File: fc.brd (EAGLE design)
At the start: 55 x 40 mm, 72 parts, among them IC1 BN055, J1 USBC, U1 LMZ21700, U2 ATMEGA2560-16AU100A-M, U4 FT230XQ, Y1 16MHz, Y2 32.768kHz

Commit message: atmega breakout cleanup
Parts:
- moved S1 37.6 mm to (12.4, 43.5)
- moved R3 36.2 mm to (12.2, 46.6)
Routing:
- net !RESET: track 38.8 -> 9.92 mm, vias 3 -> 1
- net +3V3: track 138.4 -> 128.1 mm
- net BNO_INT: track 26.6 -> 23.1 mm
- net PPM2: track 29.2 -> 32.3 mm
- net PPM0: track 37.6 -> 39.5 mm
- net PPM1: track 33.8 -> 35.3 mm
- net MOSI: track 18.6 -> 19.8 mm, vias 0 -> 1
- net SCK: track 18.2 -> 17.3 mm
- net PPM7: track 36.0 -> 35.3 mm
- net USB_TX: track 28.2 -> 27.5 mm
- net PPM3: track 29.3 -> 28.7 mm

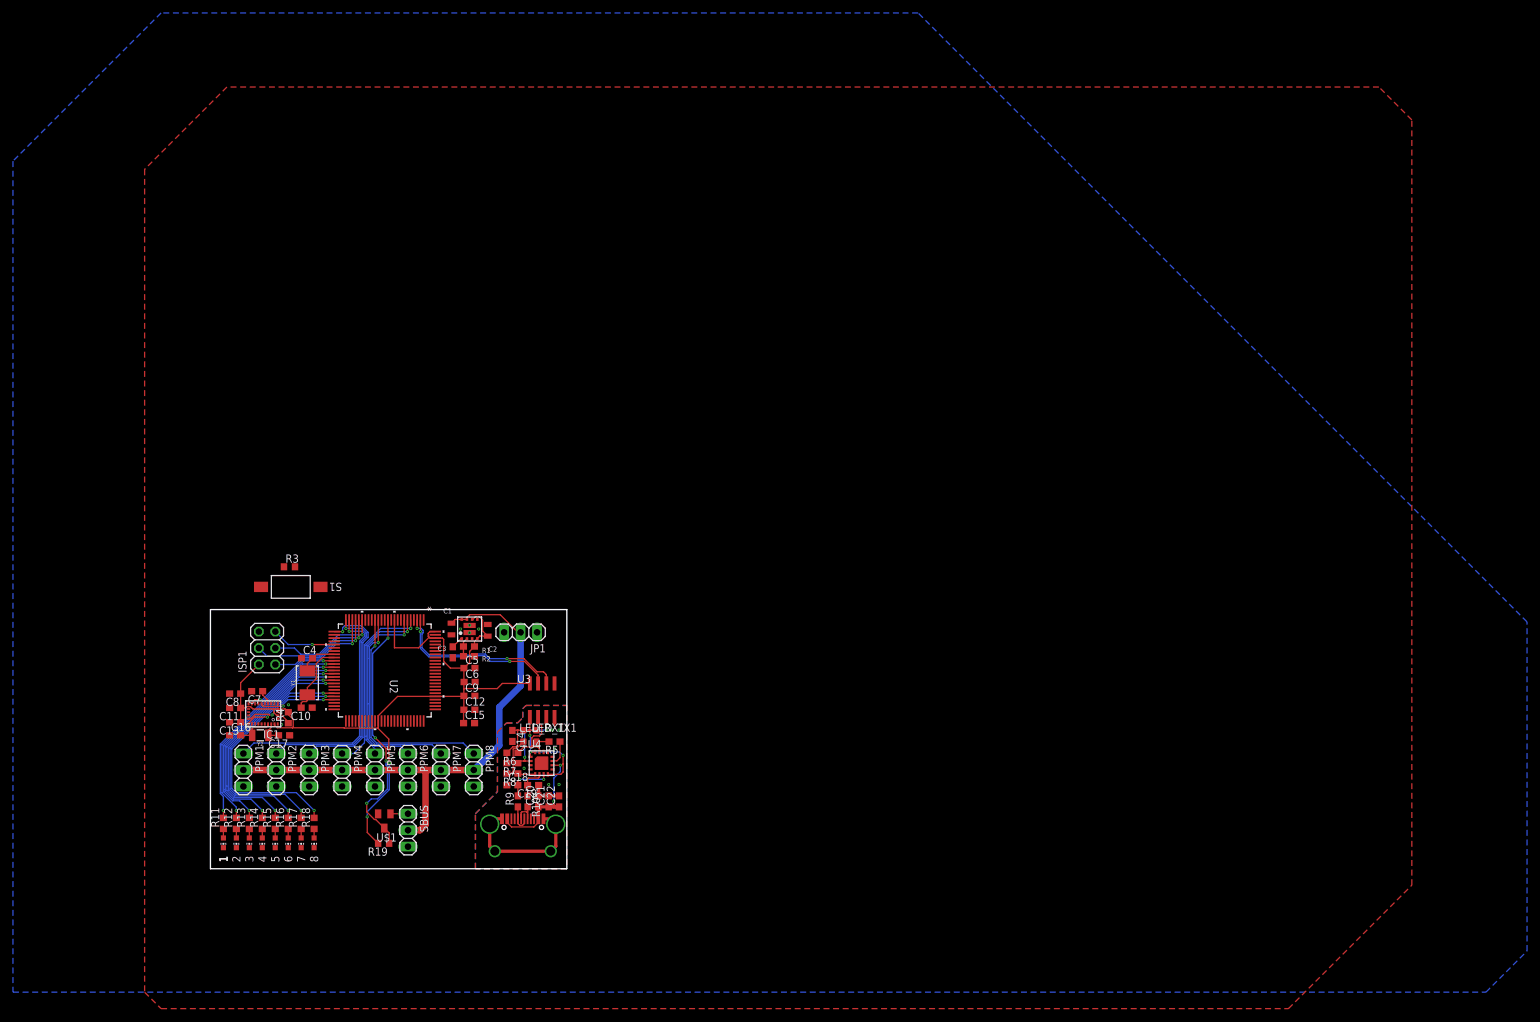
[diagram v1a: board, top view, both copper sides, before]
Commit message: isp, reset button, gnd polygon
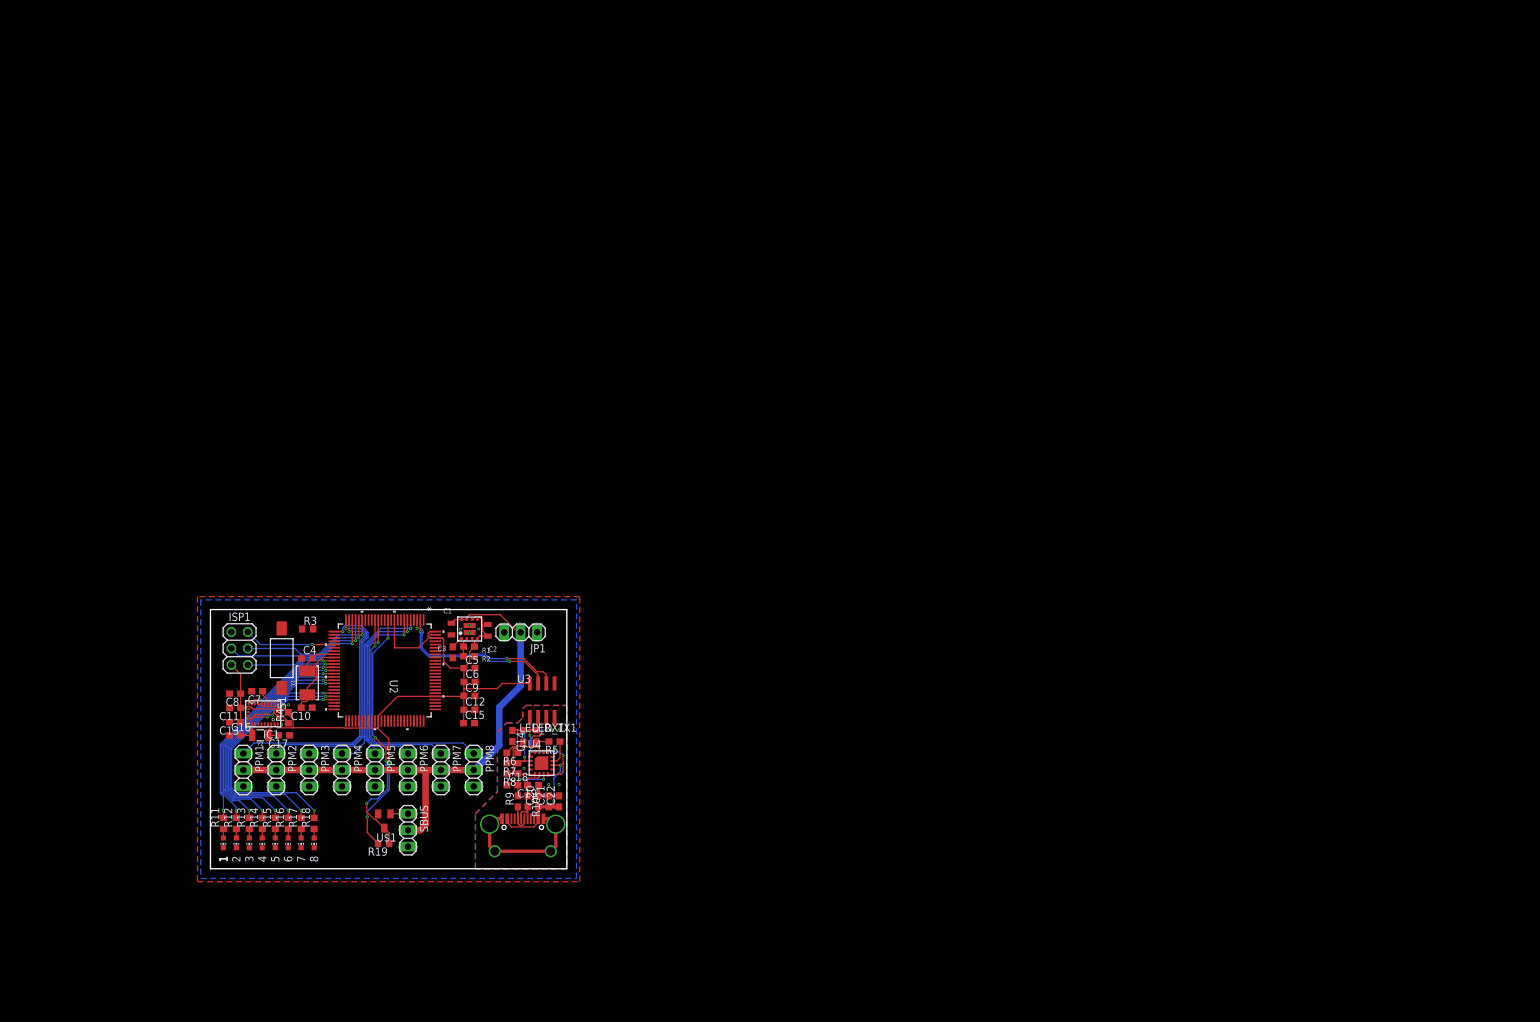
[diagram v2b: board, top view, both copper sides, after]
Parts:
- moved S1 11.1 mm to (11.0, 32.5), turned to 90 degrees
- moved R3 10.0 mm to (15.0, 37.0)
- moved ISP1 4.24 mm to (4.50, 34.0)
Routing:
- net MISO: track 17.1 -> 21.4 mm
- net SCK: track 17.3 -> 21.5 mm
- net MOSI: track 19.8 -> 24.0 mm
- net !RESET: track 9.92 -> 14.1 mm
- net +3V3: track 128.1 -> 127.5 mm
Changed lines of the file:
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@@
 <layer number="45" name="Holes" color="7" fill="1" visible="yes" active="yes"/>
 <layer number="46" name="Milling" color="3" fill="1" visible="no" active="yes"/>
-<layer number="47" name="Measures" color="7" fill="1" visible="no" active="yes"/>
+<layer number="47" name="Measures" color="7" fill="1" visible="yes" active="yes"/>
 <layer number="48" name="Document" color="7" fill="1" visible="no" active="yes"/>
 <layer number="49" name="Reference" color="7" fill="1" visible="no" active="yes"/>
@@
 <wire x1="55" y1="40" x2="0" y2="40" width="0" layer="20"/>
 <wire x1="0" y1="40" x2="0" y2="0" width="0" layer="20"/>
-<dimension x1="0" y1="0" x2="55.88" y2="0" x3="27.94" y3="66.04" textsize="1.778" layer="47"/>
-<dimension x1="0" y1="0" x2="0.1524" y2="41.148" x3="63.199978125" y3="20.34020625" textsize="1.778" layer="47"/>
 <text x="2" y="2" size="1.27" layer="21" rot="R90" align="center-right">1</text>
 <text x="2" y="2" size="1.27" layer="21" rot="R90" align="center-right">1</text>
@@
 <text x="14" y="2" size="1.27" layer="21" rot="R90" align="center-right">7</text>
 <text x="16" y="2" size="1.27" layer="21" rot="R90" align="center-right">8</text>
+<dimension x1="0" y1="0" x2="55" y2="0" x3="27.5" y3="-5" textsize="1.4224" layer="47" dtype="horizontal" width="0.1"/>
+<dimension x1="0" y1="40" x2="0" y2="0" x3="-14.5" y3="20" textsize="1.4224" layer="47" dtype="vertical" width="0.1"/>
 </plain>
 <attributes>
@@
 <attribute name="VENDOR" value="Atmel" x="26.9" y="30.6" size="1.778" layer="27" rot="R270" display="off"/>
 </element>
-<element name="ISP1" library="pinhead" library_urn="urn:adsk.eagle:library:325" package="2X03" package3d_urn="urn:adsk.eagle:package:22462/2" value="" x="8.7436" y="34.0612" smashed="yes" rot="R90">
-<attribute name="NAME" x="5.5686" y="30.2512" size="1.27" layer="25" ratio="10" rot="R90"/>
-<attribute name="VALUE" x="13.1886" y="30.2512" size="1.27" layer="27" rot="R90"/>
+<element name="ISP1" library="pinhead" library_urn="urn:adsk.eagle:library:325" package="2X03" package3d_urn="urn:adsk.eagle:package:22462/2" value="" x="4.5" y="34" smashed="yes" rot="R90">
+<attribute name="NAME" x="4.5" y="38.25" size="1.27" layer="25" ratio="10" align="bottom-center"/>
+<attribute name="VALUE" x="8.945" y="30.19" size="1.27" layer="27" rot="R90"/>
 </element>
 <element name="Y1" library="SparkFun-Clocks" library_urn="urn:adsk.eagle:library:511" package="CRYSTAL-SMD-5X3.2-2PAD" package3d_urn="urn:adsk.eagle:package:37520/1" value="16MHz" x="14.954" y="28.7012" smashed="yes" rot="R90">
@@
 <attribute name="VALUE" x="39.3274" y="24.7778" size="1.27" layer="27"/>
 </element>
-<element name="R3" library="resistor" library_urn="urn:adsk.eagle:library:348" package="R0603" package3d_urn="urn:adsk.eagle:package:23555/2" value="10k" x="12.2" y="46.6" smashed="yes">
-<attribute name="NAME" x="11.565" y="47.235" size="1.27" layer="25"/>
-<attribute name="VALUE" x="11.565" y="44.695" size="1.27" layer="27"/>
-</element>
-<element name="S1" library="switch" package="SWITCH_FSMSM" value="FSMSM" x="12.4" y="43.5" smashed="yes" rot="R180">
-<attribute name="MANUFACTURER_PART_NUMBER" value="FSMSM" x="12.4" y="43.5" size="1.778" layer="27" rot="R180" display="off"/>
-<attribute name="NAME" x="20.2994" y="44.135" size="1.27" layer="25" ratio="6" rot="SR180"/>
-<attribute name="VENDOR" value="TE Connectivity" x="12.4" y="43.5" size="1.778" layer="27" rot="R180" display="off"/>
+<element name="R3" library="resistor" library_urn="urn:adsk.eagle:library:348" package="R0603" package3d_urn="urn:adsk.eagle:package:23555/2" value="10k" x="15" y="37" smashed="yes">
+<attribute name="NAME" x="14.365" y="37.635" size="1.27" layer="25"/>
+<attribute name="VALUE" x="14.365" y="35.095" size="1.27" layer="27"/>
+</element>
+<element name="S1" library="switch" package="SWITCH_FSMSM" value="FSMSM" x="11" y="32.5" smashed="yes" rot="R90">
+<attribute name="MANUFACTURER_PART_NUMBER" value="FSMSM" x="11" y="32.5" size="1.778" layer="27" rot="R90" display="off"/>
+<attribute name="NAME" x="11.635" y="24.6006" size="1.27" layer="25" ratio="6" rot="SR90"/>
+<attribute name="VENDOR" value="TE Connectivity" x="11" y="32.5" size="1.778" layer="27" rot="R90" display="off"/>
 </element>
 <element name="C19" library="SparkFun-Capacitors" library_urn="urn:adsk.eagle:library:510" package="0603" package3d_urn="urn:adsk.eagle:package:37414/1" value="47pF" x="49.8" y="12.9" smashed="yes" rot="R180">
@@
 <contactref element="S1" pad="2"/>
 <wire x1="19.1022" y1="34.6" x2="15.6972" y2="34.6" width="0.1524" layer="1"/>
-<wire x1="10.0136" y1="36.6012" x2="12.0148" y2="34.6" width="0.1524" layer="16"/>
-<wire x1="12.0148" y1="34.6" x2="15.6972" y2="34.6" width="0.1524" layer="16"/>
+<wire x1="5.77" y1="36.54" x2="7.71" y2="34.6" width="0.1524" layer="16"/>
+<wire x1="7.71" y1="34.6" x2="15.6972" y2="34.6" width="0.1524" layer="16"/>
 <via x="15.6972" y="34.6" extent="1-16" drill="0.2"/>
-<wire x1="7.81" y1="43.5" x2="11.35" y2="46.6" width="0" layer="19" extent="1-1"/>
-<wire x1="10.0136" y1="36.6012" x2="7.81" y2="43.5" width="0" layer="19" extent="1-1"/>
+<wire x1="11" y1="37.09" x2="14.15" y2="37" width="0" layer="19" extent="1-1"/>
+<wire x1="5.77" y1="36.54" x2="11" y2="37.09" width="0" layer="19" extent="1-1"/>
 </signal>
 <signal name="+5V">
@@
 <contactref element="LED8" pad="C"/>
 <polygon width="0.1524" layer="1" rank="6">
-<vertex x="-10.16" y="107.95"/>
-<vertex x="-10.16" y="-19.05"/>
-<vertex x="-7.62" y="-21.59"/>
-<vertex x="166.37" y="-21.59"/>
-<vertex x="185.42" y="-2.54"/>
-<vertex x="185.42" y="115.57"/>
-<vertex x="180.34" y="120.65"/>
-<vertex x="2.54" y="120.65"/>
+<vertex x="-2" y="42"/>
+<vertex x="-2" y="-2"/>
+<vertex x="57" y="-2"/>
+<vertex x="57" y="42"/>
 </polygon>
 <polygon width="0.1524" layer="16" rank="6">
-<vertex x="-13.97" y="125.73"/>
-<vertex x="-30.48" y="109.22"/>
-<vertex x="-30.48" y="-19.05"/>
-<vertex x="196.85" y="-19.05"/>
-<vertex x="203.2" y="-12.7"/>
-<vertex x="203.2" y="38.1"/>
-<vertex x="109.22" y="132.08"/>
-<vertex x="-7.62" y="132.08"/>
+<vertex x="-1.5" y="41.5"/>
+<vertex x="-1.5" y="-1.5"/>
+<vertex x="56.5" y="-1.5"/>
+<vertex x="56.5" y="41.5"/>
 </polygon>
 <contactref element="JP1" pad="1"/>
@@
 <via x="40" y="36.4" extent="1-16" drill="0.2"/>
 <via x="40" y="37.6" extent="1-16" drill="0.2"/>
-<wire x1="16.99" y1="43.5" x2="19.1022" y2="33.6" width="0" layer="19" extent="1-1"/>
+<wire x1="11" y1="27.91" x2="19.1022" y2="33.6" width="0" layer="19" extent="1-1"/>
 </signal>
 <signal name="USB_RX">
@@
 <wire x1="25.8704" y1="21.6704" x2="25.8292" y2="21.7116" width="0.2032" layer="1"/>
 <wire x1="25.8292" y1="21.7116" x2="20.67679375" y2="21.7116" width="0.2032" layer="1"/>
-<wire x1="7.4736" y1="31.5212" x2="4.66" y2="28.7076" width="0.2032" layer="1"/>
-<wire x1="4.66" y1="28.7076" x2="4.66" y2="27.03" width="0.2032" layer="1"/>
+<wire x1="3.23" y1="31.46" x2="4.66" y2="30.03" width="0.2032" layer="1"/>
+<wire x1="4.66" y1="30.03" x2="4.66" y2="27.03" width="0.2032" layer="1"/>
 <wire x1="25.9" y1="22.8022" x2="25.9" y2="21.7" width="0.2032" layer="1"/>
 <wire x1="25.9" y1="21.7" x2="25.8704" y2="21.6704" width="0.2032" layer="1"/>
@@
 <wire x1="41.9984" y1="38.37670625" x2="41.47350625" y2="38.9016" width="0.2032" layer="1"/>
 <wire x1="41.9984" y1="36.7016" x2="41.9984" y2="38.37670625" width="0.2032" layer="1"/>
-<wire x1="19.1022" y1="34.1" x2="13.05" y2="46.6" width="0" layer="19" extent="1-1"/>
+<wire x1="19.1022" y1="34.1" x2="15.85" y2="37" width="0" layer="19" extent="1-1"/>
 <wire x1="28.4" y1="34.1" x2="19.1022" y2="34.1" width="0" layer="19" extent="1-1"/>
 </signal>
@@
 <contactref element="U2" pad="22"/>
 <wire x1="16.94510625" y1="32.6048" x2="14.1794625" y2="32.6048" width="0.1524" layer="16"/>
-<wire x1="10.0136" y1="31.5212" x2="13.0958625" y2="31.5212" width="0.1524" layer="16"/>
-<wire x1="13.0958625" y1="31.5212" x2="14.1794625" y2="32.6048" width="0.1524" layer="16"/>
+<wire x1="5.77" y1="31.46" x2="13.0346625" y2="31.46" width="0.1524" layer="16"/>
+<wire x1="13.0346625" y1="31.46" x2="14.1794625" y2="32.6048" width="0.1524" layer="16"/>
 <via x="22.4" y="35.2" extent="1-16" drill="0.2"/>
 <wire x1="22.4" y1="38.3978" x2="22.4" y2="35.2" width="0.1524" layer="1"/>
@@
 <contactref element="ISP1" pad="3"/>
 <contactref element="U2" pad="20"/>
-<wire x1="10.0136" y1="34.0612" x2="12.9692" y2="34.0612" width="0.1524" layer="16"/>
-<wire x1="12.9692" y1="34.0612" x2="13.9208" y2="33.1096" width="0.1524" layer="16"/>
+<wire x1="5.77" y1="34" x2="13.0304" y2="34" width="0.1524" layer="16"/>
+<wire x1="13.0304" y1="34" x2="13.9208" y2="33.1096" width="0.1524" layer="16"/>
 <wire x1="16.73600625" y1="33.1096" x2="13.9208" y2="33.1096" width="0.1524" layer="16"/>
 <wire x1="23.4" y1="38.3978" x2="23.4" y2="36.1" width="0.1524" layer="1"/>
@@
 <contactref element="ISP1" pad="4"/>
 <contactref element="U2" pad="21"/>
-<wire x1="8.6776" y1="32.8572" x2="7.4736" y2="34.0612" width="0.1524" layer="16"/>
-<wire x1="16.84055625" y1="32.8572" x2="8.6776" y2="32.8572" width="0.1524" layer="16"/>
+<wire x1="4.3728" y1="32.8572" x2="3.23" y2="34" width="0.1524" layer="16"/>
+<wire x1="16.84055625" y1="32.8572" x2="4.3728" y2="32.8572" width="0.1524" layer="16"/>
 <wire x1="22.9" y1="38.3978" x2="22.9" y2="35.65" width="0.1524" layer="1"/>
 <via x="22.9" y="35.65" extent="1-16" drill="0.2"/>

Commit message: reset, alignment, caps
reset button
aligned sbus inverter to grid
moved decoupling cap to sensible position
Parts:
- moved C15 27.7 mm to (15.0, 34.5), turned to 180 degrees
- moved S1 1.50 mm to (11.0, 34.0)
- moved U$1 0.89 mm to (27.0, 6.50)
- moved R19 0.58 mm to (27.0, 3.40)
- moved R3 0.50 mm to (15.0, 36.5), turned to 180 degrees
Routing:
- net +3V3: track 127.5 -> 132.5 mm
- net !SBUS: track 39.8 -> 38.0 mm
- net !RESET: track 14.1 -> 15.9 mm, vias 1 -> 0

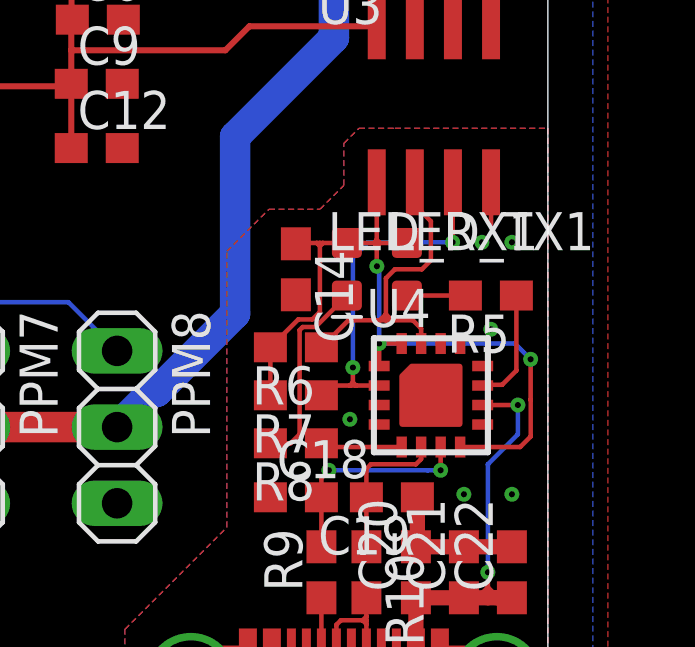
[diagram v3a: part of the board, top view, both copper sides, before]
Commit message: minor changes to usb layout
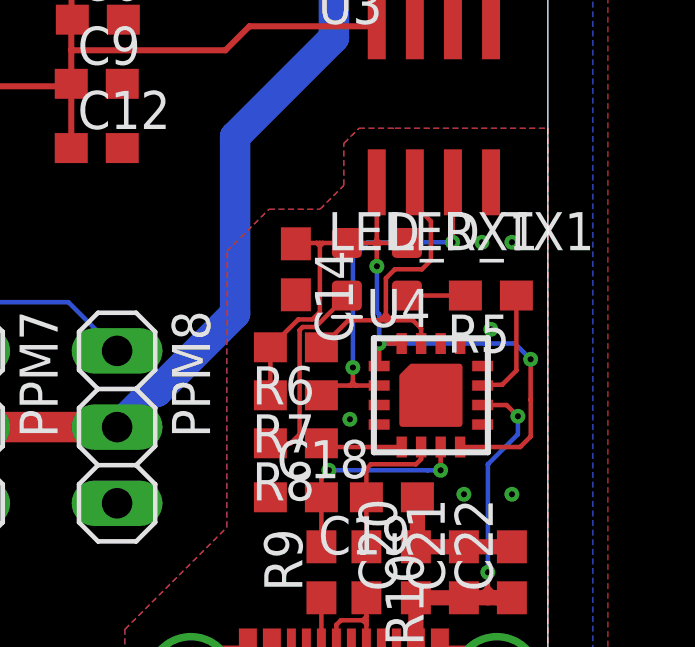
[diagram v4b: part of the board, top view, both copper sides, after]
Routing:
- net GNDIO: track 28.9 -> 27.6 mm
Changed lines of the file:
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@@
 <wire x1="53.3" y1="9.55" x2="53.8" y2="9.55" width="0.508" layer="1"/>
 <wire x1="50.6" y1="7.705" x2="50.6" y2="9.55" width="0.508" layer="1"/>
-<wire x1="52.825" y1="15.975" x2="54" y2="15.975" width="0.1524" layer="1"/>
-<via x="54" y="15.975" extent="1-16" drill="0.2"/>
 <wire x1="53.8" y1="9.55" x2="53.8" y2="9.6" width="0.1524" layer="1"/>
 <via x="53" y="10.4" extent="1-16" drill="0.2"/>
 <wire x1="53" y1="10.4" x2="53" y2="14" width="0.1524" layer="16"/>
-<wire x1="54" y1="15" x2="54" y2="15.975" width="0.1524" layer="16"/>
-<wire x1="53" y1="14" x2="54" y2="15" width="0.1524" layer="16"/>
+<wire x1="54" y1="15" x2="53" y2="14" width="0.1524" layer="16"/>
 <wire x1="53" y1="10.4" x2="53" y2="9.9" width="0.1524" layer="1"/>
 <wire x1="53" y1="9.9" x2="53" y2="9.55" width="0.1524" layer="1"/>
@@
 <wire x1="53" y1="9.9" x2="53.3" y2="9.6" width="0.1524" layer="1"/>
 <wire x1="53.3" y1="9.6" x2="53.3" y2="9.55" width="0.1524" layer="1"/>
+<wire x1="52.825" y1="15.975" x2="53.625" y2="15.975" width="0.1524" layer="1"/>
+<wire x1="53.625" y1="15.975" x2="54" y2="15.6" width="0.1524" layer="1"/>
+<via x="54" y="15.6" extent="1-16" drill="0.2"/>
+<wire x1="54" y1="15.6" x2="54" y2="15" width="0.1524" layer="16"/>
 </signal>
 <signal name="VCCIO">
@@
 <wire x1="49.295" y1="21.482" x2="49.295" y2="21.472" width="0.1524" layer="1"/>
 <wire x1="49.295" y1="21.472" x2="49.2" y2="21.377" width="0.1524" layer="1"/>
-<wire x1="49.375" y1="18.025" x2="49.375" y2="20.525" width="0.1524" layer="16"/>
-<wire x1="49.375" y1="20.525" x2="49.3" y2="20.6" width="0.1524" layer="16"/>
+<wire x1="49.375" y1="18.025" x2="49.375" y2="19" width="0.1524" layer="16"/>
 <via x="49.3" y="20.6" extent="1-16" drill="0.2"/>
 <wire x1="49.3" y1="20.6" x2="49.295" y2="20.605" width="0.1524" layer="1"/>
@@
 <wire x1="47.4" y1="21.277" x2="47.3" y2="21.377" width="0.1524" layer="1"/>
 <wire x1="47.4" y1="21.277" x2="47.5" y2="21.377" width="0.1524" layer="1"/>
+<wire x1="49.375" y1="19" x2="49.3" y2="19.075" width="0.1524" layer="16"/>
+<wire x1="49.3" y1="19.075" x2="49.3" y2="20.6" width="0.1524" layer="16"/>
 </signal>
 <signal name="GNDIO">
@@
 <wire x1="50.35" y1="11.5" x2="50.6" y2="11.25" width="0.1524" layer="1"/>
 <wire x1="52.075" y1="18.2258125" x2="52.075" y2="18.025" width="0.1524" layer="1"/>
-<wire x1="53.105" y1="23.4" x2="53.105" y2="22.005" width="0.1524" layer="1"/>
 <contactref element="C22" pad="2"/>
 <wire x1="50.6" y1="11.25" x2="52.2" y2="11.25" width="0.508" layer="1"/>
